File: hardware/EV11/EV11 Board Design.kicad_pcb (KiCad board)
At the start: 4 copper layers, 72.7 x 89.4 mm, 110 parts, among them J1 Conn_01x02_Socket, J10 Conn_01x08_Socket, J11 Conn_01x06_Female, J13 Conn_01x04_Female, J2 Conn_01x02_Female, J5 Conn_01x02_Socket, J7 Conn_01x04_Female, J8 Conn_01x06_Female, J9 USB_C_Receptacle, SW4 SW_Push, SW5 SW_Push, U1 STM32F405RGTx, U11 ESP32-S3-WROOM-1-N8R2, U13 BM14B(0.8)-24DS-0.4V(53), U2 BQ21040DBVR, U3 CH340C, U4 USBLC6-2P6, U5 STM32F030C8Tx, U6 WM8960CGEFL/RV, U7 TPS63060, Y1 Crystal_GND24

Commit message: EV11 files
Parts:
- removed C27: 1u, Capacitor_SMD:C_0402_1005Metric
- removed J2: Conn_01x02_Female, Connector_JST:JST_PH_S2B-PH-SM4-TB_1x02-1MP_P2.00mm_Horizontal
- removed J8: Conn_01x06_Female, Connector_JST:JST_PH_S6B-PH-SM4-TB_1x06-1MP_P2.00mm_Horizontal
- removed REF** (x5): MountingHole_2.1mm, MountingHole:MountingHole_2.1mm
- added J4: AudioPlug4, PJ_313E_8A:PJ_313E_8A, F.Cu at (130.8, 58.1)
- moved R10 52.9 mm to (173.9, 125.1), turned to 0 degrees
- moved C36 50.4 mm to (173.9, 124.1), turned to 0 degrees
- moved J13 48.9 mm to (180.6, 64.6), turned to 90 degrees
- moved C35 29.9 mm to (176.9, 105.8), turned to -90 degrees
- moved R13 0.80 mm to (140.9, 64.0)
- moved R14 0.80 mm to (139.9, 64.0)
- moved R15 0.80 mm to (138.9, 64.0)
- moved U4 0.07 mm to (157.9, 129.9), turned to 90 degrees
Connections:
- D1 pad 1: Net-(D1-K) -> /BATTERY_MON
- U2 pad 3: Net-(D1-K) -> /BATTERY_MON
- U6 pad 19: unconnected-(U6-SPK_RN-Pad19) -> /SPK_RN
- U6 pad 22: unconnected-(U6-SPK_RP-Pad22) -> /SPK_RP
- U6 pad 4: Net-(U6-LINPUT1) -> unconnected-(U6-LINPUT1-Pad4)
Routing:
- net /MIC_N: track 79.0 -> 0.00 mm, vias 2 -> 0
- net /HP_R: track 26.8 -> 68.4 mm, vias 2 -> 4
- net /BATTERY_MON: track 28.6 -> 70.0 mm, vias 0 -> 4
- net /HP_L: track 29.6 -> 70.9 mm, vias 2 -> 4
- net Net-(D1-K): track 23.6 -> 0.00 mm, vias 2 -> 0
- net GND: track 566.8 -> 552.7 mm
- net /SPK_LP: track 11.1 -> 0.00 mm, vias 2 -> 0
- net /BTN_UI: track 81.7 -> 71.3 mm, vias 4 -> 6
- net /SPK_LN: track 10.3 -> 0.00 mm, vias 2 -> 0
- net /BTN_NET: track 83.1 -> 74.4 mm
- net /MIC_P: track 86.1 -> 78.5 mm, vias 2 -> 6
- net +3.3V: track 458.1 -> 451.6 mm
- net /UI_BOOT: track 42.4 -> 47.9 mm
- net /UD-: track 7.73 -> 2.94 mm
- net /IN_3: track 80.3 -> 75.9 mm
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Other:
- board size 72.7 x 89.4 mm -> 68.4 x 89.4 mm
- board text added: "2023-12"
- board text added: "Display_CONN"
- board text added: "EV11"
- board text removed: "1"
- board text removed: "2"
- board text removed: "2023-11"
- board text removed: "3"
- board text removed: "4"
- board text removed: "5"
- board text removed: "6"
- board text removed: "BOOT_CAP"
- board text removed: "BTN_NET"
- board text removed: "BTN_RST"
- board text removed: "BTN_UI"
- board text removed: "EV10"
- board text removed: "SPEAKER_CONN"
- board text removed: "SPK_LN"
- board text removed: "SPK_LP"

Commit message: Added another test point to EV10.1 for BCLK. EV11 WIP
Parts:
- removed J9: USB_C_Receptacle, Connector_USB:USB_C_Receptacle_HRO_TYPE-C-31-M-12
- removed R2, R3: 5k1, Resistor_SMD:R_0402_1005Metric
- added R28: 5k1, Resistor_SMD:R_0402_1005Metric, F.Cu at (152.0, 134.8)
- added R29: 5k1, Resistor_SMD:R_0402_1005Metric, F.Cu at (149.0, 134.8)
- added USB-C1: TYPE-C-31-M-12, footprint:USB-C_SMD-TYPE-C-31-M-12, F.Cu at (150.3, 141.6)
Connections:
- U1 pad 52: /I2S_ADCDAT -> /KB_ROW7
- U1 pad 53: /I2S_DACDAT -> /KB_COL5
- U1 pad 56: /KB_ROW7 -> /I2S_ADCDAT
- U1 pad 57: /KB_COL5 -> /I2S_DACDAT
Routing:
- net Net-(J9-CC1): track 4.17 -> 0.00 mm
- net Net-(J9-CC2): track 3.99 -> 0.00 mm
- net Net-(USB-C1-CC1): track 0.00 -> 3.89 mm
- net Net-(USB-C1-CC2): track 0.00 -> 3.87 mm
- net /I2S_ADCDAT: track 28.4 -> 26.6 mm
- net GND: track 552.7 -> 554.3 mm
- net /I2S_DACDAT: track 26.8 -> 25.5 mm
- net /MGMT_NRST: track 117.8 -> 116.6 mm
- net /DISP_CS: track 94.1 -> 94.7 mm
- net /KB_COL5: track 26.6 -> 27.2 mm
- net /USB_TX1_MGMT: track 61.5 -> 62.0 mm
- net /USB_RX1_MGMT: track 59.6 -> 60.1 mm
- net /USB_DTR: track 59.0 -> 59.5 mm
- net /DISP_RSTR: track 85.8 -> 86.3 mm
- net /USB_RTS: track 44.5 -> 45.1 mm
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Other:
- outline, holes or cut-outs redrawn

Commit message: Began working on updates to EV11
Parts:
- removed J13: Conn_01x04_Female, 1x4 pin download:1x4pin 1mm connector
- removed R28, R29: 5k1, Resistor_SMD:R_0402_1005Metric
- removed USB-C1: TYPE-C-31-M-12, footprint:USB-C_SMD-TYPE-C-31-M-12
- added J2: Conn_01x06_Female, Connector_JST:JST_PH_S6B-PH-SM4-TB_1x06-1MP_P2.00mm_Horizontal, F.Cu at (198.7, 60.1)
- added J3: Conn_01x06_Female, Connector_JST:JST_PH_S6B-PH-SM4-TB_1x06-1MP_P2.00mm_Horizontal, F.Cu at (198.7, 71.4)
- added J9: USB_C_Receptacle, Connector_USB:USB_C_Receptacle_HRO_TYPE-C-31-M-12, F.Cu at (150.3, 143.0)
- added R2: 5k1, Resistor_SMD:R_0402_1005Metric, F.Cu at (152.1, 134.5)
- added R3: 5k1, Resistor_SMD:R_0402_1005Metric, F.Cu at (149.1, 134.5)
- moved J4 92.0 mm to (165.5, 143.3), turned to 90 degrees
- moved J11 65.3 mm to (199.0, 84.1)
- moved D3 0.11 mm to (139.5, 61.8)
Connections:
- C42 pad 1: Net-(J5-Pin_1) -> Net-(SW1-B)
- C43 pad 1: Net-(J5-Pin_1) -> Net-(SW1-B)
- C44 pad 1: Net-(J5-Pin_1) -> Net-(SW1-B)
- C45 pad 1: Net-(J5-Pin_1) -> Net-(SW1-B)
- C46 pad 1: Net-(J5-Pin_1) -> Net-(SW1-B)
- C47 pad 1: Net-(J5-Pin_1) -> Net-(SW1-B)
- C48 pad 1: Net-(J5-Pin_1) -> Net-(SW1-B)
- D18 pad 2: +3.3V -> Net-(D18-GK)
- D18 pad 4: Net-(D18-GK) -> +3.3V
- D3 pad 2: +3.3V -> Net-(D3-GK)
- D3 pad 4: Net-(D3-GK) -> +3.3V
- D4 pad 2: +3.3V -> Net-(D4-A)
- D4 pad 4: Net-(D4-GK) -> +3.3V
- D5 pad 2: +3.3V -> Net-(D5-A)
- D5 pad 4: Net-(D5-GK) -> +3.3V
- J4 pad R1: /HP_R -> (no net)
- J4 pad R2: /IN_3 -> (no net)
- J4 pad S: /HP_L -> (no net)
- J4 pad T: /MIC_P -> (no net)
- R17 pad 2: Net-(D4-GK) -> Net-(D4-A)
- R19 pad 2: Net-(J5-Pin_1) -> Net-(SW1-B)
- R21 pad 2: Net-(J5-Pin_1) -> Net-(SW1-B)
- R24 pad 2: Net-(D5-GK) -> Net-(D5-A)
- U1 pad 52: /KB_ROW7 -> /I2S_ADCDAT
- U1 pad 53: /KB_COL5 -> /I2S_DACDAT
- U1 pad 56: /I2S_ADCDAT -> /KB_ROW7
- U1 pad 57: /I2S_DACDAT -> /KB_COL5
- U6 pad 19: /SPK_RN -> unconnected-(U6-SPK_RN-Pad19)
- U6 pad 22: /SPK_RP -> unconnected-(U6-SPK_RP-Pad22)
- U6 pad 23: /SPK_LN -> unconnected-(U6-SPK_LN-Pad23)
- U6 pad 25: /SPK_LP -> unconnected-(U6-SPK_LP-Pad25)
- U6 pad 28: unconnected-(U6-AGND-Pad28) -> GND
- U7 pad 9: Net-(J5-Pin_1) -> Net-(SW1-B)
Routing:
- net /MIC_P: track 78.5 -> 0.00 mm, vias 6 -> 0
- net /IN_3: track 75.9 -> 0.00 mm, vias 4 -> 0
- net /MGMT_SWCLK: track 73.2 -> 0.00 mm, vias 4 -> 0
- net /HP_L: track 70.9 -> 0.00 mm, vias 4 -> 0
- net /HP_R: track 68.4 -> 0.00 mm, vias 4 -> 0
- net /MGMT_SWDIO: track 67.7 -> 0.00 mm, vias 4 -> 0
- net /MGMT_NRST: track 116.6 -> 74.0 mm, vias 8 -> 4
- net /MGMT_BOOT: track 126.8 -> 102.0 mm, vias 6 -> 5
- net /BTN_NET: track 74.4 -> 51.0 mm, vias 6 -> 5
- net /BTN_UI: track 71.3 -> 48.4 mm, vias 6 -> 5
- net /BTN_RST: track 68.0 -> 46.0 mm, vias 4 -> 3
- net Net-(SW1-B): track 0.00 -> 19.4 mm, vias 0 -> 2
- net Net-(J5-Pin_1): track 170.6 -> 151.2 mm, vias 4 -> 2
- net GND: track 554.3 -> 543.0 mm, vias 154 -> 152
- net Net-(J9-CC1): track 0.00 -> 4.17 mm
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- added copper zone on F.Cu, net Net-(SW1-B)
- removed copper zone on F.Cu, net Net-(J5-Pin_1)
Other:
- outline, holes or cut-outs redrawn
- board text added: "BRETT REGNIER"
- board text removed: "FINN BERG"

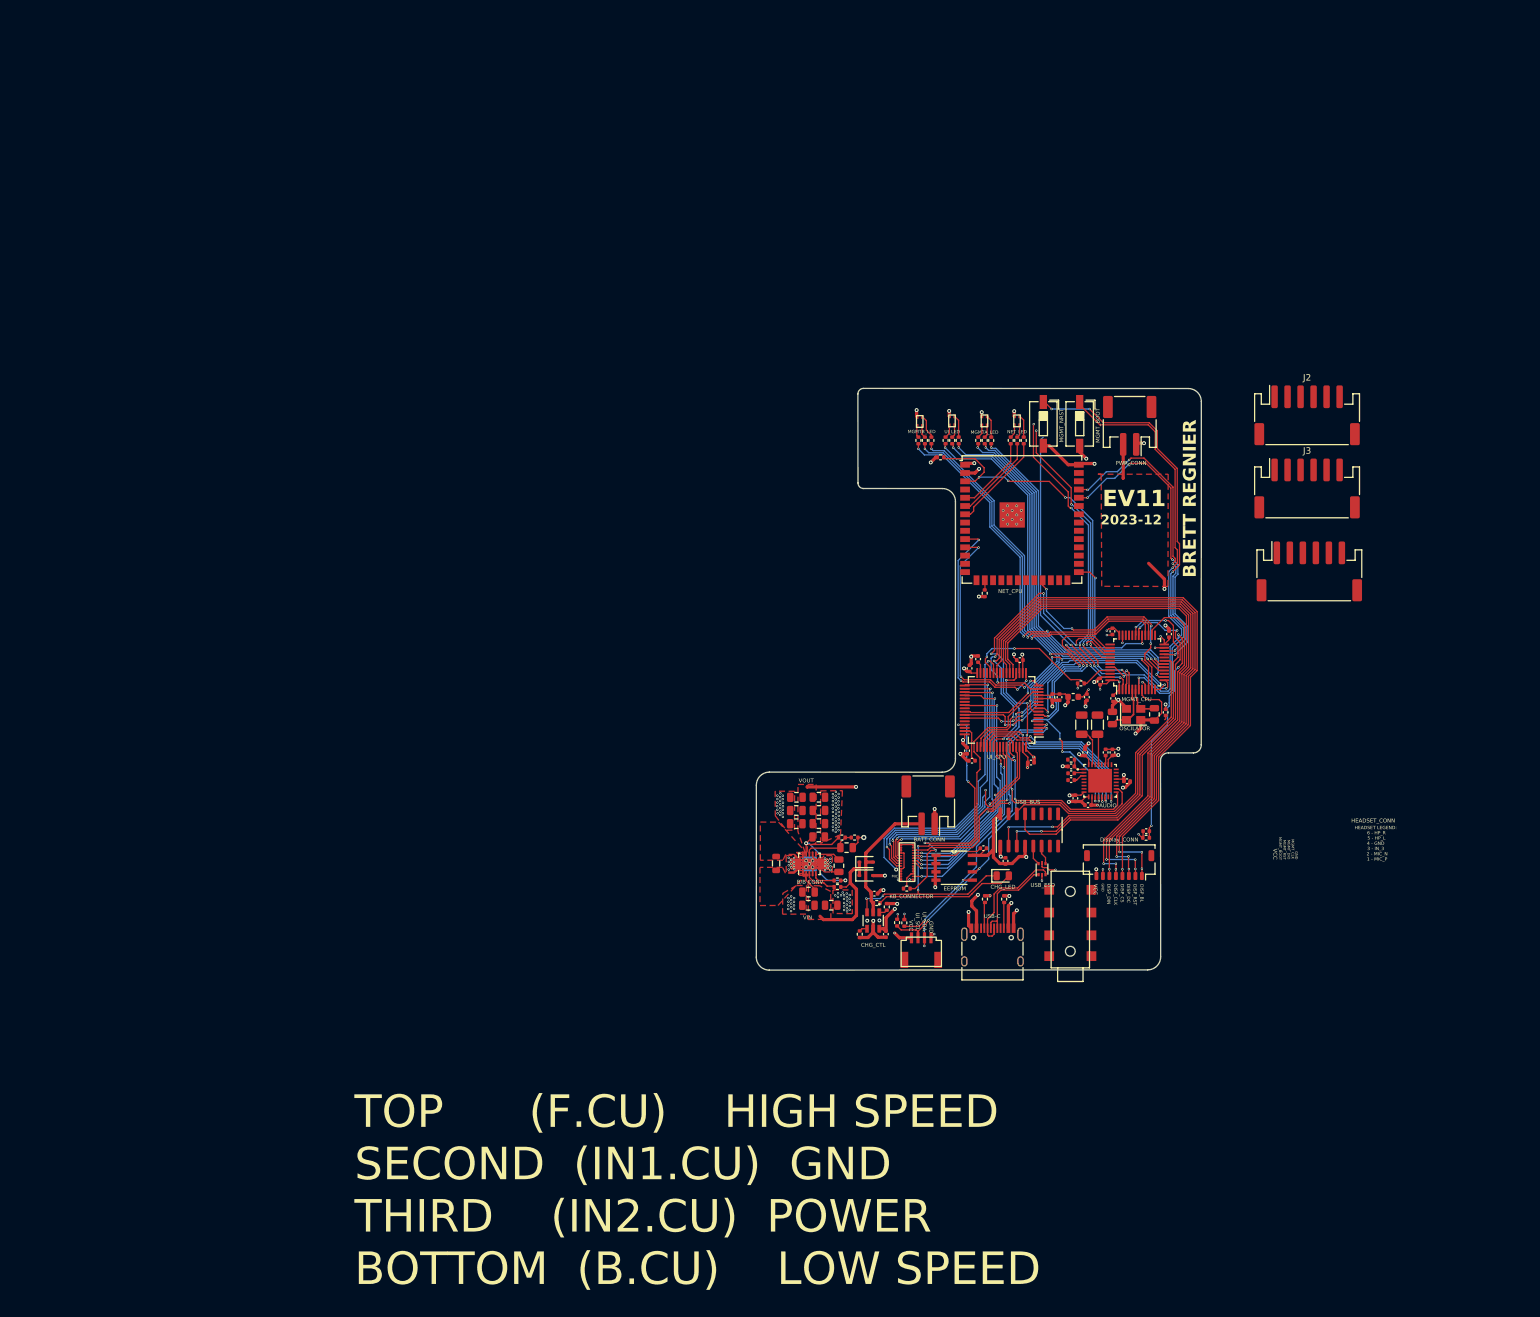
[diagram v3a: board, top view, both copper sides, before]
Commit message: Resizing board and trying to clean up rats nest
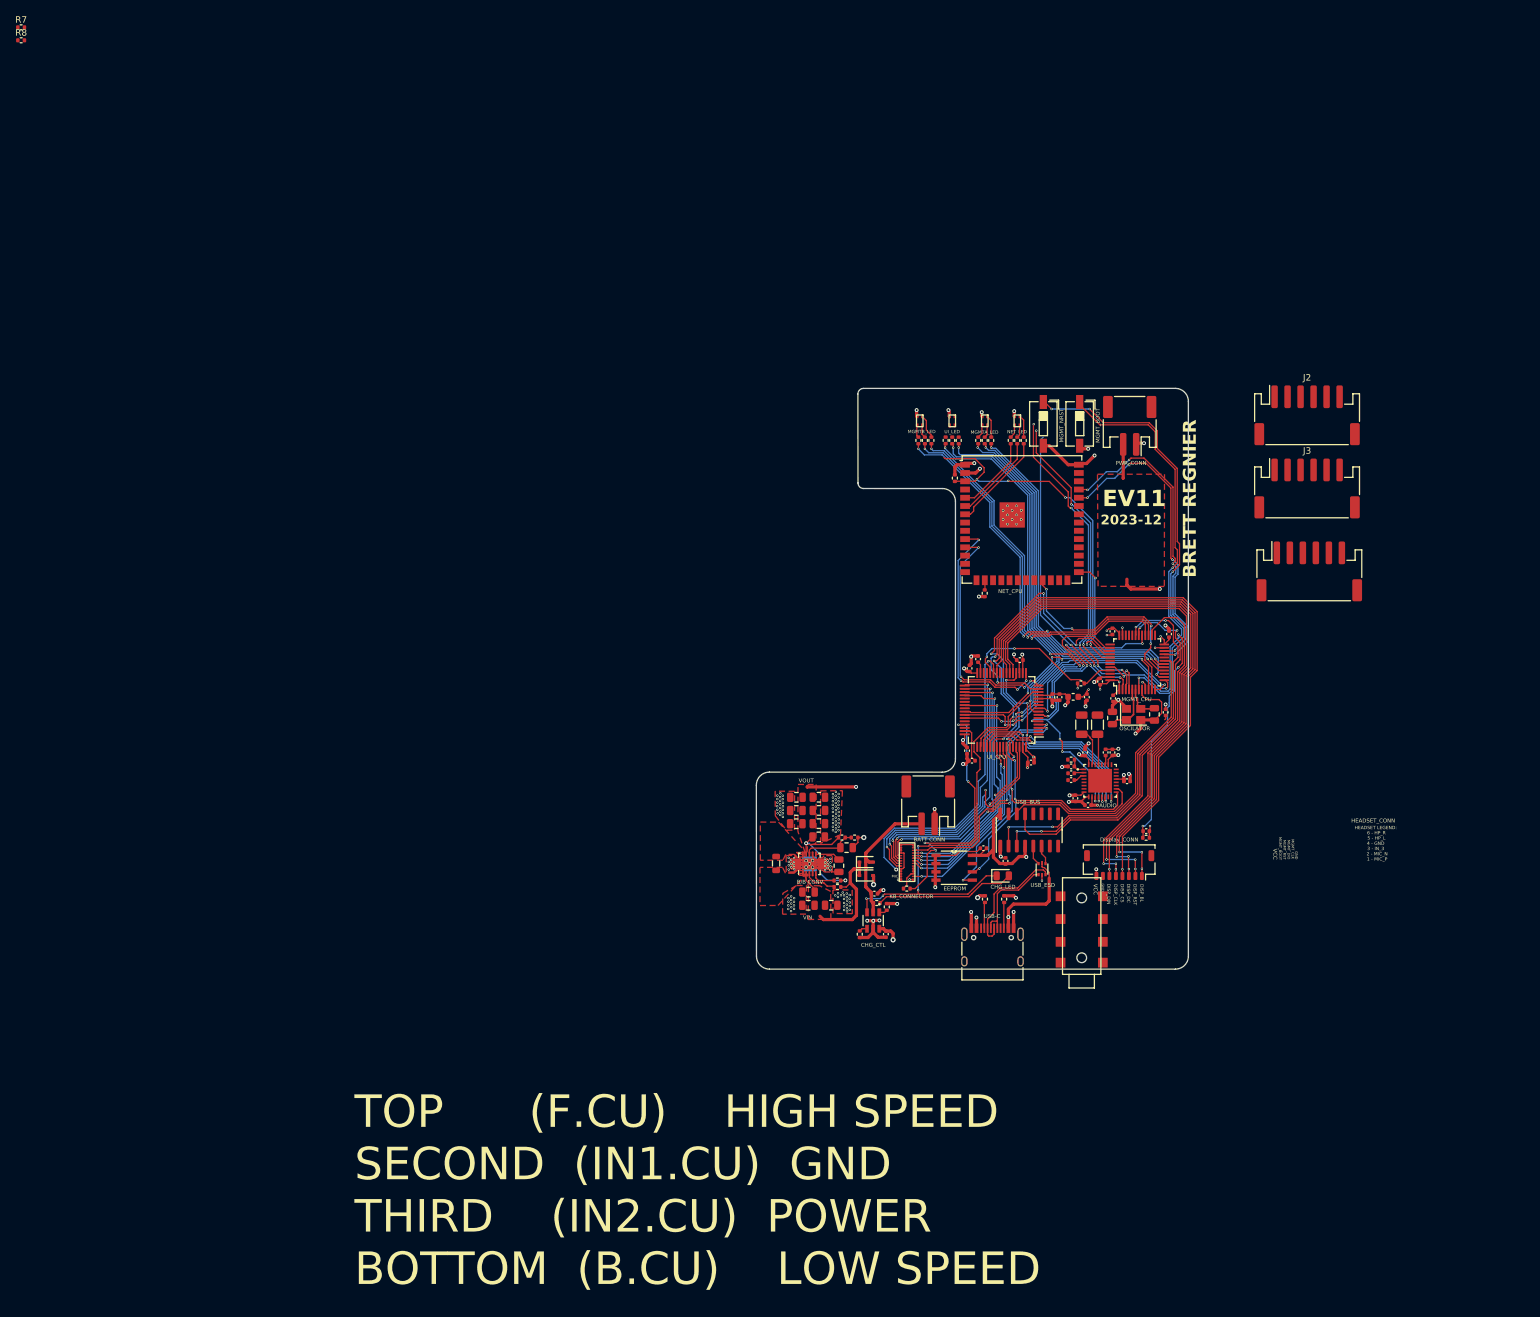
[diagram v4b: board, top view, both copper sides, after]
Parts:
- removed J7: Conn_01x04_Female, 1x4 pin download:1x4pin 1mm connector
- moved R7 193.4 mm to (0.95, 0.49), turned to 0 degrees
- moved R8 191.1 mm to (0.95, 2.48), turned to 0 degrees
- moved R4 3.88 mm to (144.5, 69.8), turned to 90 degrees
- moved R25 2.02 mm to (145.1, 64.0)
- moved J4 2.02 mm to (167.3, 144.3)
- moved R23 2.01 mm to (143.1, 64.0)
- moved D3 1.70 mm to (138.7, 60.3), turned to -90 degrees
- moved D18 1.59 mm to (148.7, 60.3), turned to -90 degrees
- moved D4 1.59 mm to (153.7, 60.3), turned to -90 degrees
- moved D5 1.59 mm to (143.7, 60.3), turned to -90 degrees
- turned C36 to 180 degrees
- turned R10 to 180 degrees
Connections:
- U1 pad 54: /UI_LED_B -> /UI_LED_R
- U1 pad 9: /UI_LED_R -> /UI_LED_B
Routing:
- net +3.3V: track 452.8 -> 329.3 mm, vias 25 -> 22
- net GND: track 543.0 -> 498.3 mm, vias 152 -> 149
- net /UI_SCL: track 61.0 -> 41.9 mm, vias 4 -> 3
- net /UI_SDA: track 65.8 -> 48.3 mm, vias 5 -> 3
- net Net-(J5-Pin_1): track 151.2 -> 166.6 mm
- net Net-(D5-BK): track 3.46 -> 0.00 mm
- net Net-(D5-RK): track 2.03 -> 0.02 mm
- net Net-(D4-GK): track 0.00 -> 1.95 mm
- net /NET_RST: track 55.5 -> 57.2 mm
- net /UI_LED_B: track 60.7 -> 59.1 mm
- net /UI_LED_R: track 59.8 -> 61.3 mm
- net /MGMT_BOOT: track 102.0 -> 102.7 mm
- net /UI_LED_G: track 53.2 -> 53.8 mm
- net VBUS: vias 5 -> 4
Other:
- board size 68.4 x 89.4 mm -> 66.4 x 89.3 mm
- board text removed: "UI_SCL"
- board text removed: "UI_SDA"
